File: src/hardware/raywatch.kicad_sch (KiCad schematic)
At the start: 0 parts

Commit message: Created microcontroller page
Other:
- added sheet MC: Microcontroller (microcontroller.kicad_sch)
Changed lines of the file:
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@@
 	(generator_version "9.0")
 	(paper "A4")
+	(sheet
+		(at 21.59 52.07)
+		(size 12.7 3.81)
+		(exclude_from_sim no)
+		(in_bom yes)
+		(on_board yes)
+		(dnp no)
+		(fields_autoplaced yes)
+		(stroke
+			(width 0.1524)
+			(type solid)
+		)
+		(fill
+			(color 0 0 0 0.0000)
+		)
+		(property "Sheetname" "MC: Microcontroller"
+			(at 21.59 51.3584 0)
+			(effects
+				(font
+					(size 1.27 1.27)
+				)
+				(justify left bottom)
+			)
+		)
+		(property "Sheetfile" "microcontroller.kicad_sch"
+			(at 21.59 56.4646 0)
+			(effects
+				(font
+					(size 1.27 1.27)
+				)
+				(justify left top)
+			)
+		)
+		(instances
+			(project "raywatch"
+				(path "/7b654ee8-2a53-4d39-8b7d-32c7bb3cb0ed"
+					(page "2")
+				)
+			)
+		)
+	)
 	(sheet_instances
 		(path "/"

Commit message: Added GPIO Extensions
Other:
- title: (none) -> Raywatch
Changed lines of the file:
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@@
 	(generator_version "9.0")
 	(paper "A4")
+	(title_block
+		(title "Raywatch")
+		(date "2026-10-21")
+	)
 	(sheet
 		(at 21.59 52.07)

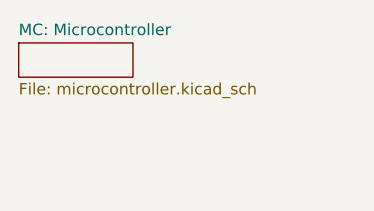
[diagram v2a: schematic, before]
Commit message: Added another GPIO Expander
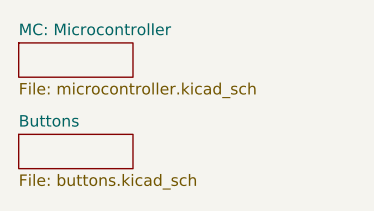
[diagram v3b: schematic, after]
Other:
- added sheet Buttons (buttons.kicad_sch)
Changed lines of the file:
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@@
+	)
+	(sheet
+		(at 21.59 62.23)
+		(size 12.7 3.81)
+		(exclude_from_sim no)
+		(in_bom yes)
+		(on_board yes)
+		(dnp no)
+		(fields_autoplaced yes)
+		(stroke
+			(width 0.1524)
+			(type solid)
+		)
+		(fill
+			(color 0 0 0 0.0000)
+		)
+		(property "Sheetname" "Buttons"
+			(at 21.59 61.5184 0)
+			(effects
+				(font
+					(size 1.27 1.27)
+				)
+				(justify left bottom)
+			)
+		)
+		(property "Sheetfile" "buttons.kicad_sch"
+			(at 21.59 66.6246 0)
+			(effects
+				(font
+					(size 1.27 1.27)
+				)
+				(justify left top)
+			)
+		)
+		(instances
+			(project "raywatch"
+				(path "/7b654ee8-2a53-4d39-8b7d-32c7bb3cb0ed"
+					(page "4")
+				)
+			)
+		)
 	)
 	(sheet

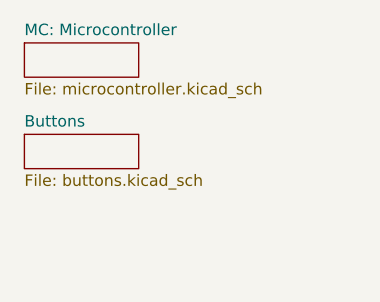
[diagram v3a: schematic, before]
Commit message: Added display
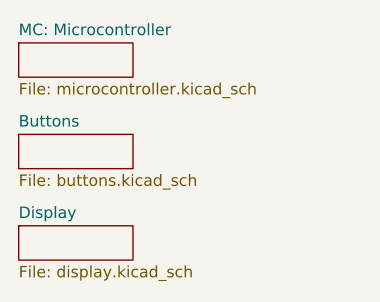
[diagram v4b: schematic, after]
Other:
- added sheet Display (display.kicad_sch)
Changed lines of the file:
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@@
 	)
 	(sheet
-		(at 21.59 62.23)
+		(at 20.955 72.39)
+		(size 12.7 3.81)
+		(exclude_from_sim no)
+		(in_bom yes)
+		(on_board yes)
+		(dnp no)
+		(fields_autoplaced yes)
+		(stroke
+			(width 0.1524)
+			(type solid)
+		)
+		(fill
+			(color 0 0 0 0.0000)
+		)
+		(property "Sheetname" "Display"
+			(at 20.955 71.6784 0)
+			(effects
+				(font
+					(size 1.27 1.27)
+				)
+				(justify left bottom)
+			)
+		)
+		(property "Sheetfile" "display.kicad_sch"
+			(at 20.955 76.7846 0)
+			(effects
+				(font
+					(size 1.27 1.27)
+				)
+				(justify left top)
+			)
+		)
+		(instances
+			(project "raywatch"
+				(path "/7b654ee8-2a53-4d39-8b7d-32c7bb3cb0ed"
+					(page "5")
+				)
+			)
+		)
+	)
+	(sheet
+		(at 20.955 62.23)
 		(size 12.7 3.81)
 		(exclude_from_sim no)
@@
 		)
 		(property "Sheetname" "Buttons"
-			(at 21.59 61.5184 0)
+			(at 20.955 61.5184 0)
 			(effects
 				(font
@@
 		)
 		(property "Sheetfile" "buttons.kicad_sch"
-			(at 21.59 66.6246 0)
+			(at 20.955 66.6246 0)
 			(effects
 				(font
@@
 	)
 	(sheet
-		(at 21.59 52.07)
+		(at 20.955 52.07)
 		(size 12.7 3.81)
 		(exclude_from_sim no)
@@
 		)
 		(property "Sheetname" "MC: Microcontroller"
-			(at 21.59 51.3584 0)
+			(at 20.955 51.3584 0)
 			(effects
 				(font
@@
 		)
 		(property "Sheetfile" "microcontroller.kicad_sch"
-			(at 21.59 56.4646 0)
+			(at 20.955 56.4646 0)
 			(effects
 				(font

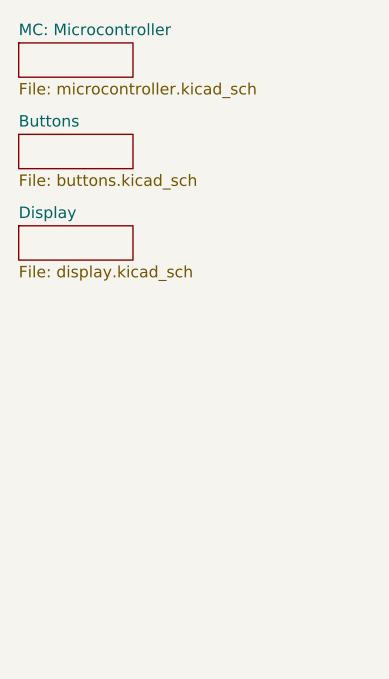
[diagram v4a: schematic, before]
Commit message: Added LEDs
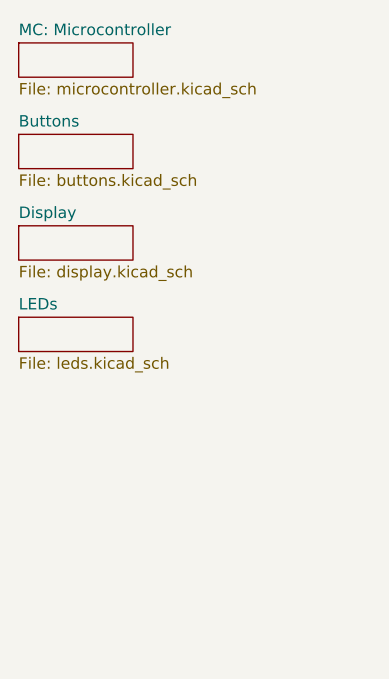
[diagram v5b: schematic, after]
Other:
- added sheet LEDs (leds.kicad_sch)
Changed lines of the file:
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@@
+	)
+	(sheet
+		(at 20.955 82.55)
+		(size 12.7 3.81)
+		(exclude_from_sim no)
+		(in_bom yes)
+		(on_board yes)
+		(dnp no)
+		(fields_autoplaced yes)
+		(stroke
+			(width 0.1524)
+			(type solid)
+		)
+		(fill
+			(color 0 0 0 0.0000)
+		)
+		(property "Sheetname" "LEDs"
+			(at 20.955 81.8384 0)
+			(effects
+				(font
+					(size 1.27 1.27)
+				)
+				(justify left bottom)
+			)
+		)
+		(property "Sheetfile" "leds.kicad_sch"
+			(at 20.955 86.9446 0)
+			(effects
+				(font
+					(size 1.27 1.27)
+				)
+				(justify left top)
+			)
+		)
+		(instances
+			(project "raywatch"
+				(path "/7b654ee8-2a53-4d39-8b7d-32c7bb3cb0ed"
+					(page "6")
+				)
+			)
+		)
 	)
 	(sheet

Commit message: Added accelerometer and second I²C bus
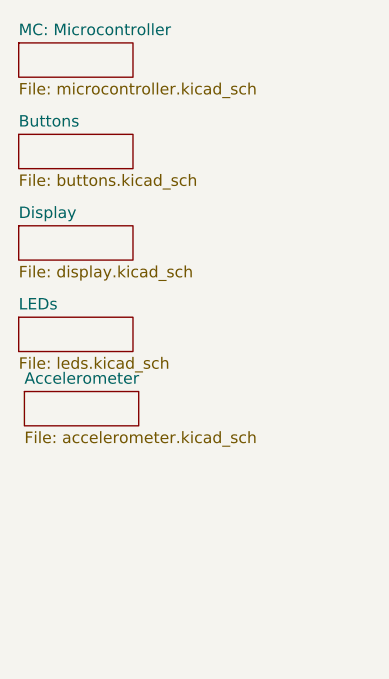
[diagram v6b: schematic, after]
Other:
- added sheet Accelerometer (accelerometer.kicad_sch)
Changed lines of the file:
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@@
+	)
+	(sheet
+		(at 21.59 90.805)
+		(size 12.7 3.81)
+		(exclude_from_sim no)
+		(in_bom yes)
+		(on_board yes)
+		(dnp no)
+		(fields_autoplaced yes)
+		(stroke
+			(width 0.1524)
+			(type solid)
+		)
+		(fill
+			(color 0 0 0 0.0000)
+		)
+		(property "Sheetname" "Accelerometer"
+			(at 21.59 90.0934 0)
+			(effects
+				(font
+					(size 1.27 1.27)
+				)
+				(justify left bottom)
+			)
+		)
+		(property "Sheetfile" "accelerometer.kicad_sch"
+			(at 21.59 95.1996 0)
+			(effects
+				(font
+					(size 1.27 1.27)
+				)
+				(justify left top)
+			)
+		)
+		(instances
+			(project "raywatch"
+				(path "/7b654ee8-2a53-4d39-8b7d-32c7bb3cb0ed"
+					(page "8")
+				)
+			)
+		)
 	)
 	(sheet

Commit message: Added microSD slot
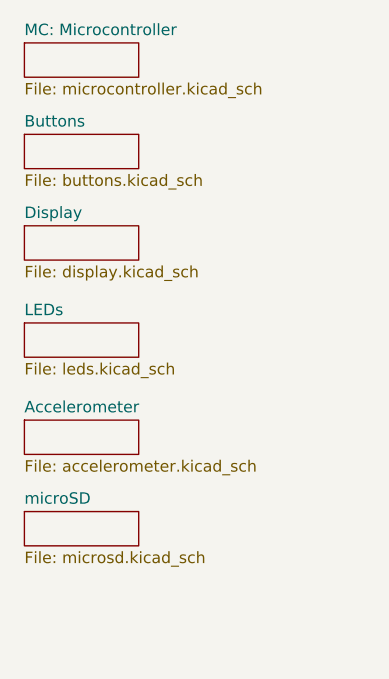
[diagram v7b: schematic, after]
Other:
- added sheet microSD (microsd.kicad_sch)
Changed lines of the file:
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@@
 	)
 	(sheet
-		(at 20.955 72.39)
+		(at 21.59 72.39)
 		(size 12.7 3.81)
 		(exclude_from_sim no)
@@
 		)
 		(property "Sheetname" "Display"
-			(at 20.955 71.6784 0)
+			(at 21.59 71.6784 0)
 			(effects
 				(font
@@
 		)
 		(property "Sheetfile" "display.kicad_sch"
-			(at 20.955 76.7846 0)
+			(at 21.59 76.7846 0)
 			(effects
 				(font
@@
 	)
 	(sheet
-		(at 20.955 82.55)
+		(at 21.59 83.185)
 		(size 12.7 3.81)
 		(exclude_from_sim no)
@@
 		)
 		(property "Sheetname" "LEDs"
-			(at 20.955 81.8384 0)
+			(at 21.59 82.4734 0)
 			(effects
 				(font
@@
 		)
 		(property "Sheetfile" "leds.kicad_sch"
-			(at 20.955 86.9446 0)
+			(at 21.59 87.5796 0)
 			(effects
 				(font
@@
 	)
 	(sheet
-		(at 21.59 90.805)
+		(at 21.59 93.98)
 		(size 12.7 3.81)
 		(exclude_from_sim no)
@@
 		)
 		(property "Sheetname" "Accelerometer"
-			(at 21.59 90.0934 0)
+			(at 21.59 93.2684 0)
 			(effects
 				(font
@@
 		)
 		(property "Sheetfile" "accelerometer.kicad_sch"
-			(at 21.59 95.1996 0)
+			(at 21.59 98.3746 0)
 			(effects
 				(font
@@
 	)
 	(sheet
-		(at 20.955 62.23)
+		(at 21.59 104.14)
+		(size 12.7 3.81)
+		(exclude_from_sim no)
+		(in_bom yes)
+		(on_board yes)
+		(dnp no)
+		(fields_autoplaced yes)
+		(stroke
+			(width 0.1524)
+			(type solid)
+		)
+		(fill
+			(color 0 0 0 0.0000)
+		)
+		(property "Sheetname" "microSD"
+			(at 21.59 103.4284 0)
+			(effects
+				(font
+					(size 1.27 1.27)
+				)
+				(justify left bottom)
+			)
+		)
+		(property "Sheetfile" "microsd.kicad_sch"
+			(at 21.59 108.5346 0)
+			(effects
+				(font
+					(size 1.27 1.27)
+				)
+				(justify left top)
+			)
+		)
+		(instances
+			(project "raywatch"
+				(path "/7b654ee8-2a53-4d39-8b7d-32c7bb3cb0ed"
+					(page "9")
+				)
+			)
+		)
+	)
+	(sheet
+		(at 21.59 62.23)
 		(size 12.7 3.81)
 		(exclude_from_sim no)
@@
 		)
 		(property "Sheetname" "Buttons"
-			(at 20.955 61.5184 0)
+			(at 21.59 61.5184 0)
 			(effects
 				(font
@@
 		)
 		(property "Sheetfile" "buttons.kicad_sch"
-			(at 20.955 66.6246 0)
+			(at 21.59 66.6246 0)
 			(effects
 				(font
@@
 	)
 	(sheet
-		(at 20.955 52.07)
+		(at 21.59 52.07)
 		(size 12.7 3.81)
 		(exclude_from_sim no)
@@
 		)
 		(property "Sheetname" "MC: Microcontroller"
-			(at 20.955 51.3584 0)
+			(at 21.59 51.3584 0)
 			(effects
 				(font
@@
 		)
 		(property "Sheetfile" "microcontroller.kicad_sch"
-			(at 20.955 56.4646 0)
-			(effects
-				(font
+			(at 21.59 56.4646 0)
+			(effects
+				(font

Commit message: Added heartrate & O2 sensor
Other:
- added sheet Heartrate & O₂ (heartrate_and_o2.kicad_sch)
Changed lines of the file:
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@@
+	)
+	(sheet
+		(at 21.59 114.3)
+		(size 12.7 3.81)
+		(exclude_from_sim no)
+		(in_bom yes)
+		(on_board yes)
+		(dnp no)
+		(fields_autoplaced yes)
+		(stroke
+			(width 0.1524)
+			(type solid)
+		)
+		(fill
+			(color 0 0 0 0.0000)
+		)
+		(property "Sheetname" "Heartrate & O₂"
+			(at 21.59 113.5884 0)
+			(effects
+				(font
+					(size 1.27 1.27)
+				)
+				(justify left bottom)
+			)
+		)
+		(property "Sheetfile" "heartrate_and_o2.kicad_sch"
+			(at 21.59 118.6946 0)
+			(effects
+				(font
+					(size 1.27 1.27)
+				)
+				(justify left top)
+			)
+		)
+		(instances
+			(project "raywatch"
+				(path "/7b654ee8-2a53-4d39-8b7d-32c7bb3cb0ed"
+					(page "10")
+				)
+			)
+		)
 	)
 	(sheet
